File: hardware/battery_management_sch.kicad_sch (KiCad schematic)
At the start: 79 parts, among them IC1 BQ7791501PWR, IC2 BQ24618RGER, Q100 DMP3036SSD, Q2 PMOS, U1 RQ3E100BN, U2 RQ3E100BN, U3 RQ3E100BN, U4 RQ3E100BN

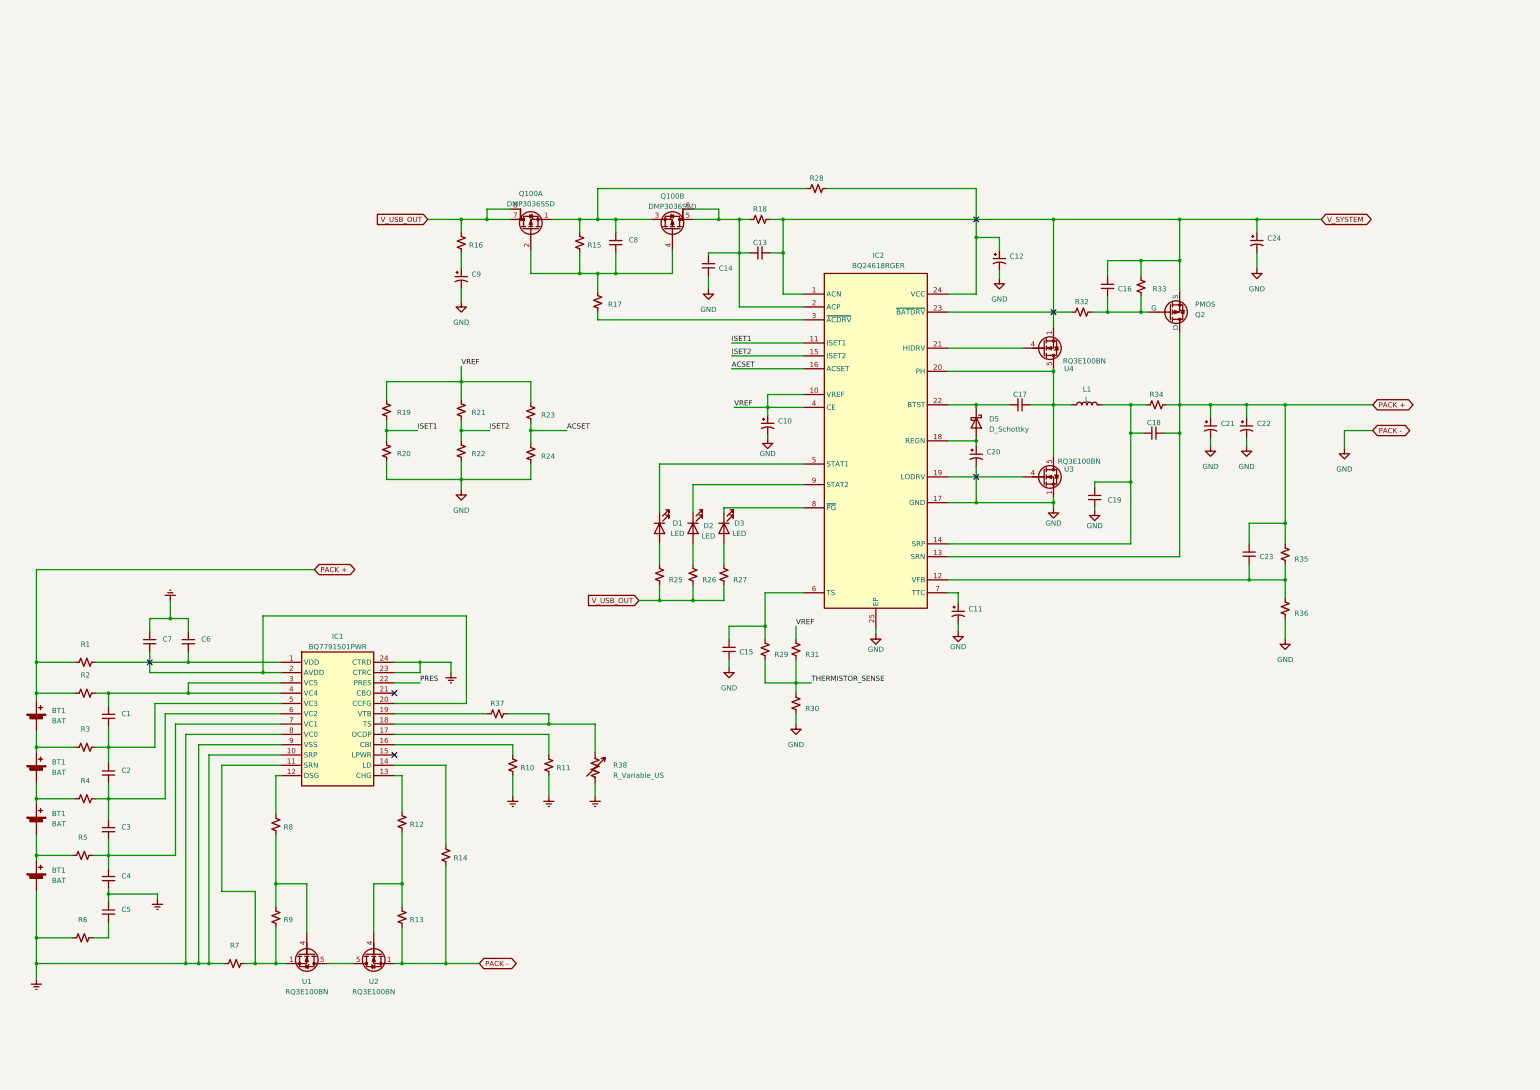
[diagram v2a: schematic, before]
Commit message: Component values chosen for bat. charge, bat. protect, USB input
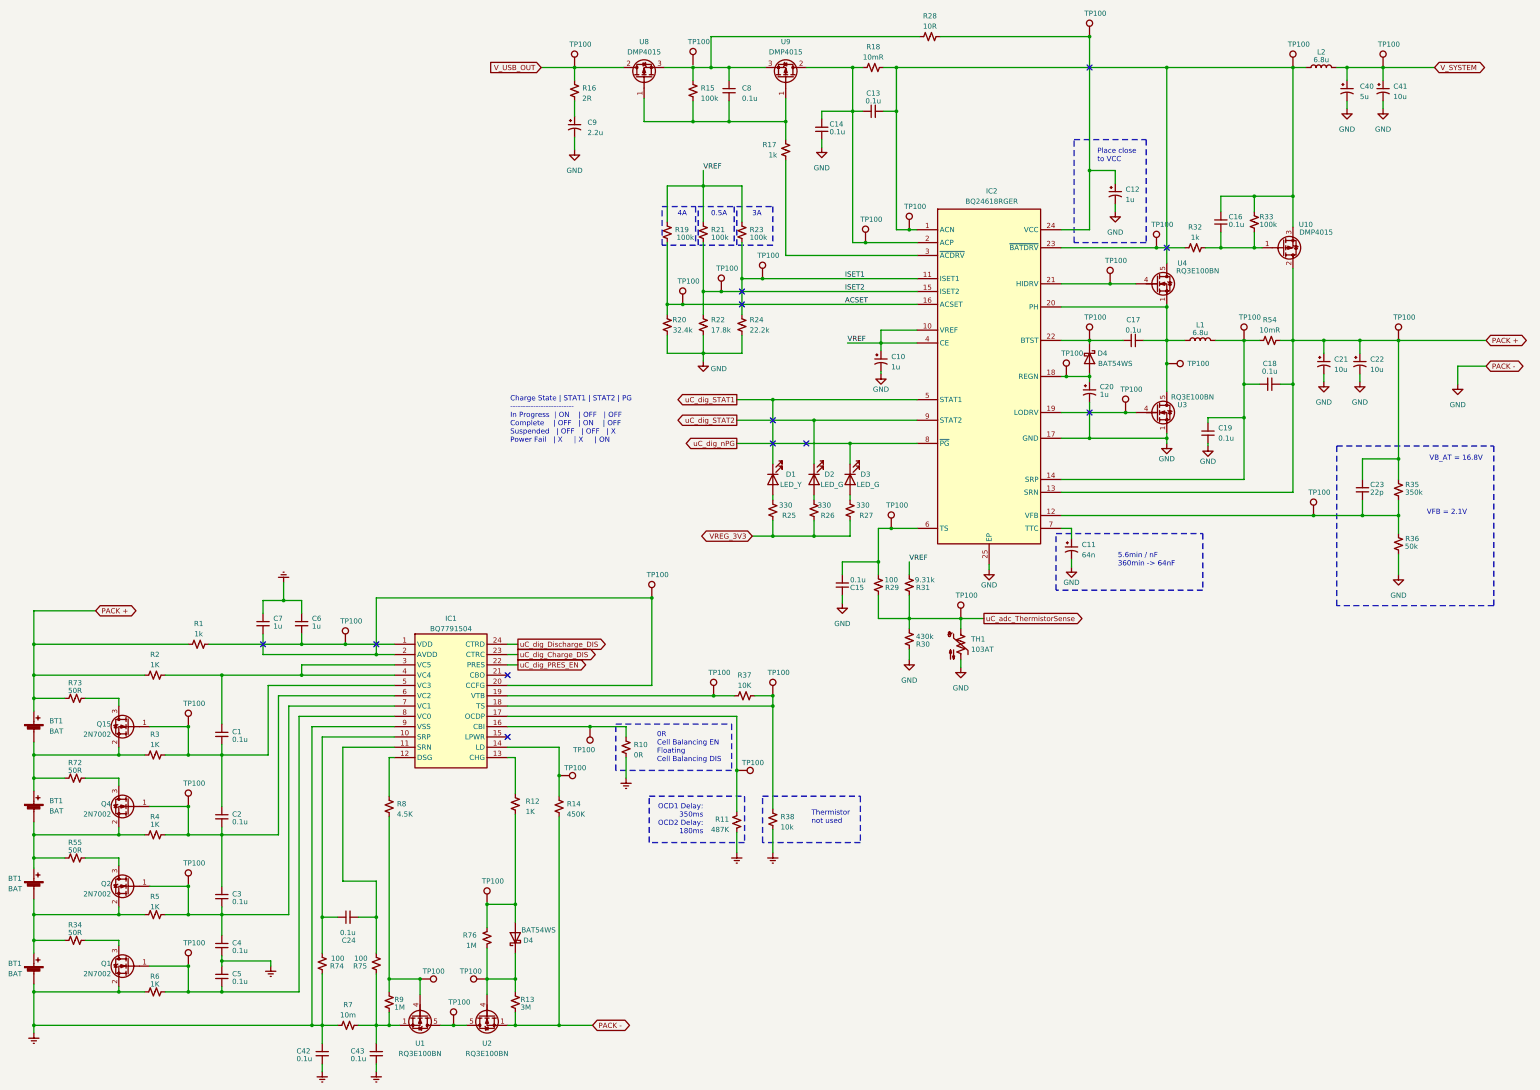
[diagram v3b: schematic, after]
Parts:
- removed C24: ~, symbol Device:C_Polarized_Small_US
- removed D5: D_Schottky, symbol Device:D_Schottky
- removed Q100: DMP3036SSD, Package_SO:SO-8_3.9x4.9mm_P1.27mm, symbol Device:Q_Dual_PMOS_S1G1S2G2D2D2D1D1
- removed Q2: PMOS, symbol Simulation_SPICE:PMOS
- removed R38: R_Variable_US, symbol Device:R_Variable_US
- added C24, C42, C43: 0.1u, Capacitor_SMD:C_0805_2012Metric, symbol Device:C_Small
- added C40: 5u, symbol Device:C_Polarized_Small_US
- added C41: 10u, symbol Device:C_Polarized_Small_US
- added D4 (x2): BAT54WS, Diode_SMD:D_SOD-323_HandSoldering, symbol Device:D_Schottky
- added L2: 6.8u, Inductor_SMD:L_Bourns_SRR1260, symbol Device:L
- added Q1, Q15, Q2, Q4: 2N7002, Package_TO_SOT_SMD:SOT-23, symbol Transistor_FET:2N7002
- added R38: 10k, symbol Device:R_Small_US
- added R54: 10mR, Resistor_SMD:R_1206_3216Metric, symbol Device:R_Small_US
- added R55, R72, R73: 50R, symbol Device:R_Small_US
- added R74, R75: 100, symbol Device:R_Small_US
- added R76: 1M, symbol Device:R_Small_US
- added TH1: 103AT, User_Thermistor:Thermistor_AWG30, symbol Device:Thermistor_NTC_US
- added TP100 (x36): ~, TestPoint:TestPoint_Pad_D1.5mm, symbol Connector:TestPoint
- added U10, U8, U9: DMP4015, Package_TO_SOT_SMD:TO-252-2, symbol User_MOSFET:DMP4015
- C1, C2, C3, C4, C5: value ~ -> 0.1u; footprint (none) -> Capacitor_SMD:C_0805_2012Metric
- C10, C12, C20, C6, C7: value ~ -> 1u
- C11: value ~ -> 64n
- C13, C14, C15, C16, C17, C18, C19, C8: value ~ -> 0.1u
- C21, C22: value ~ -> 10u
- C23: value ~ -> 22p
- C9: value ~ -> 2.2u
- D1: value LED -> LED_Y; footprint (none) -> LED_SMD:LED_0805_2012Metric_Pad1.15x1.40mm_HandSolder
- D2: value LED -> LED_G
- D3: value LED -> LED_G; footprint (none) -> LED_SMD:LED_0805_2012Metric_Pad1.15x1.40mm_HandSolder
- IC1: value BQ7791501PWR -> BQ7791504; Height 1.2 -> (none); Manufacturer_Name Texas Instruments -> (none); Manufacturer_Part_Number BQ7791501PWR -> (none); Mouser Part Number 595-BQ7791501PWR -> 595-BQ7791504PW; Mouser Price/Stock https://www.mouser.co.uk/ProductDetail/Texas-Instruments/BQ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 -> https://www.mouser.com/ProductDetail/Texas-Instruments/BQ77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; Price (none) -> 2.11
- L1: value L -> 6.8u; footprint (none) -> Inductor_SMD:L_Bourns_SRR1260; Price (none) -> 0.58; Vendor (none) -> https://www.mouser.com/ProductDetail/Bourns/SRR1260A-6R8Y?q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
- R1, R17, R32: value ~ -> 1k
- R10: value ~ -> 0R
- R11: value ~ -> 487K
- R12, R2, R3, R4, R5, R6: value ~ -> 1K
- R13: value ~ -> 3M
- R14: value ~ -> 450K
- R15, R19, R21, R23, R33: value ~ -> 100k
- R16: value ~ -> 2R; footprint (none) -> Resistor_SMD:R_2010_5025Metric
- R18: value ~ -> 10mR; footprint (none) -> Resistor_SMD:R_1206_3216Metric
- R20: value ~ -> 32.4k
- R22: value ~ -> 17.8k
- R24: value ~ -> 22.2k
- R25, R26, R27: value ~ -> 330
- R28: value ~ -> 10R
- R29: value ~ -> 100
- R30: value ~ -> 430k
- R31: value ~ -> 9.31k
- R34: value ~ -> 50R
- R35: value ~ -> 350k
- R36: value ~ -> 50k
- R37: value ~ -> 10K
- R7: value ~ -> 10m
- R8: value ~ -> 4.5K
- R9: value ~ -> 1M
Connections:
- net ACSET: now also R19.2, R20.1, TP100.1; no longer R23.2, R24.1
- net Earth: now also C42.1, C42.2, C43.2, Q1.2 (S), R38.2, R74.1; no longer IC1.10 (SRP), IC1.23 (CTRC), IC1.24 (CTRD), IC1.8 (VC0)
- net GND: now also C40.2, C41.2, TH1.2
- net ISET1: now also R23.2, R24.1, TP100.1; no longer R19.2, R20.1
- net ISET2: now also TP100.1
- net PACK +: now also R54.2, R73.1, TP100.1, U10.2; no longer R34.2
- net V_SYSTEM: now also C40.1, C41.1, L2.2, TP100.1; no longer C13.2, C16.2, IC2.1 (ACN), R18.2, R33.2, U4.1, U4.2, U4.3
- net V_USB_OUT: now also TP100.1, U8.2; no longer R25.1, R26.1, R27.1
- net at C17.2, IC2.22 (BTST): now also D4.1 (K), TP100.1
- net at C20.1, IC2.18 (REGN): now also D4.2 (A), TP100.1
- net at C16.1, R32.2, R33.1: now also U10.1
- net at C8.1, R15.2, R28.1: now also U8.3, U9.3
- net at C8.2, R15.1, R17.1: now also U8.1, U9.1
- net at C13.1, C14.2, IC2.2 (ACP)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: now also TP100.1, U9.2
- net at IC2.19 (LODRV), U3.4: now also TP100.1
- net at C17.1, IC2.20 (PH), L1.1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: now also U4.1, U4.2, U4.3, TP100.1; no longer U4.5
- net at BT1.1 (+), BT1.2 (-), R3.1: now also Q15.2 (S), R72.1
- net at C1.2, C2.1, IC1.5 (VC3)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: now also Q15.1 (G), TP100.1
- net at C23.2, IC2.12 (VFB), R35.1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: now also TP100.1
- net at C15.2, IC2.6 (TS), R29.2: now also TP100.1
- net at R13.2, U2.4: now also D4.1 (K), R76.1, TP100.1; no longer R12.1
- net at U1.5, U2.5: now also TP100.1
- net at BT1.1 (+), BT1.2 (-), R4.1: now also Q4.2 (S), R55.1
- net at BT1.1 (+), BT1.2 (-), R5.1: now also R34.1, Q2.2 (S)
- net at C5.2, R6.2: now also IC1.8 (VC0), Q1.1 (G), TP100.1
- net at R7.2, R9.1, U1.1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: now also C43.1, R75.2; no longer IC1.11 (SRN)
- net at R8.1, R9.2, U1.4: now also TP100.1
- net uC_dig_nPG: now reaches D3.1 (K), IC2.8 (~{PG})
- net uC_dig_STAT2: now reaches D2.1 (K), IC2.9 (STAT2)
- net at IC1.14 (LD), R14.2: now also TP100.1
- net at IC2.23 (~{BATDRV}), R32.1: now also TP100.1
- net at C6.2, IC1.1 (VDD), R1.2: now also TP100.1
- net at C2.2, C3.1, IC1.6 (VC2)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: now also Q4.1 (G), TP100.1
- net at C3.2, C4.1, IC1.7 (VC1)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: now also Q2.1 (G), TP100.1
- net at IC1.17 (OCDP), R11.1: now also TP100.1
- net at C7.2, IC1.2 (AVDD), IC1.20 (CCFG): now also TP100.1
- net at C12.1, IC2.24 (VCC), R28.2: now also TP100.1
- net uC_dig_STAT1: now reaches D1.1 (K), IC2.5 (STAT1)
- net at IC1.19 (VTB), R37.1: now also TP100.1
- net at IC1.18 (TS), R37.2: now also R38.1, TP100.1
- net at C18.2, C19.1, IC2.14 (SRP)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: now also R54.1, TP100.1; no longer R34.1
- net at IC1.16 (CBI), R10.1: now also TP100.1
- net at IC2.21 (HIDRV), U4.4: now also TP100.1
- net PRES renamed uC_dig_PRES_EN
- net THERMISTOR_SENSE renamed uC_adc_ThermistorSense
- net uC_adc_ThermistorSense: now also TH1.1, TP100.1
- new net: Q2.3 (D), R55.2
- new net: Q1.3 (D), R34.2
- new net: C24.2, IC1.11 (SRN), R75.1
- new net: D4.2 (A), R12.1, R76.2, TP100.1
- new net: C13.2, C16.2, IC2.1 (ACN), L2.1, R18.2, R33.2, TP100.1, TP100.1, U10.3, U4.5
- new net: Q4.3 (D), R72.2
- new net: C24.1, IC1.10 (SRP), R74.2
- new net: Q15.3 (D), R73.2
- new net VREG_3V3: R25.1, R26.1, R27.1
- new net uC_dig_Charge_DIS: IC1.23 (CTRC)
- new net uC_dig_Discharge_DIS: IC1.24 (CTRD)
- no-connect marks 6 -> 12
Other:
- note added: "0.5A"
- note added: "0R Cell Balancing EN Floating Cell Balancing DIS"
- note added: "3A"
- note added: "4A"
- note added: "5.6min / nF 360min -> 64nF"
- note added: "Charge State | STAT1 | STAT2 | PG ------------------------- In Progress | ON | OFF | OFF Complete | OFF | ON | OFF Suspended | OFF | OFF | X Power Fail | X | X | ON"
- note added: "OCD1 Delay: 350ms OCD2 Delay: 180ms"
- note added: "Place close to VCC"
- note added: "Thermistor not used"
- note added: "VB_AT = 16.8V"
- note added: "VFB = 2.1V"
- moved on the sheet: BT1, C1, C10, C11, C12, C13, C14, C15, C16, C17, C18, C19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

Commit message: Most work finished on stage1. Moving on to stage2.
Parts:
- removed L2: 6.8u, Inductor_SMD:L_Bourns_SRR1260, symbol Device:L
- added C44: 0.1u, symbol Device:C_Small
- added D9: D_Zener, symbol Device:D_Zener
- added R77: 50k, symbol Device:R_Small_US
- added R78: 8.8k, symbol Device:R_Small_US
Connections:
- net GND: now also C44.1, D9.2 (A), R78.1
- net V_SYSTEM: now also C13.2, C16.2, IC2.1 (ACN), R18.2, R33.2, TP100.1, TP100.1, U10.3, U4.5
- net V_USB_OUT: now also R77.2
- new net uc_an_usbVoltage: C44.2, D9.1 (K), R77.1, R78.2
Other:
- title: (none) -> Battery Management Stage

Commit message: More simulation and work done on SEPIC stage. MOSFET changes to USB stage and charging stage.
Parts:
- removed U10, U8, U9: DMP4015, Package_TO_SOT_SMD:TO-252-2, symbol User_MOSFET:DMP4015
- added Q10: SQJ951EP, Daniel_xMOS:PowerPAK® SO-8L Dual, symbol Daniel_PMOS:Q_Dual_PMOS_S1G1S2G2D2D1
- added Q13: STL45P3LLH6, Daniel_xMOS:PowerFLAT 5x6, symbol Daniel_PMOS:Q_PMOS_DGS
- added Q6: MUN5334DW1, Package_TO_SOT_SMD:SOT-363_SC-70-6, symbol Transistor_BJT:MUN5334DW1
- added R42, R52: R_Small_US, symbol Device:R_Small_US
- D3: value LED_G -> LED_R
- renumbered BT1 to BT2, BT1 to BT3, BT1 to BT4, D4 to D5, D4 to D8, TP100 to TP1, TP100 to TP10, TP100 to TP11, TP100 to TP12, TP100 to TP13, TP100 to TP14, TP100 to TP15, TP100 to TP16, TP100 to TP17, TP100 to TP18, TP100 to TP19, TP100 to TP2, TP100 to TP20, TP100 to TP21, TP100 to TP22, TP100 to TP23, TP100 to TP24, TP100 to TP25, TP100 to TP26, TP100 to TP27, TP100 to TP28, TP100 to TP29, TP100 to TP3, TP100 to TP30, TP100 to TP31, TP100 to TP32, TP100 to TP33, TP100 to TP34, TP100 to TP35, TP100 to TP36, TP100 to TP4, TP100 to TP5, TP100 to TP6, TP100 to TP7, TP100 to TP8, TP100 to TP9
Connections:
- net GND: now also Q6.1 (E2), R52.1
- net PACK +: now also Q13.5 (D), Q13.6 (D), Q13.7 (G), Q13.8 (D), Q6.4 (E1)
- net V_SYSTEM: now also Q13.1 (S), Q13.2 (D), Q13.3 (D)
- net V_USB_OUT: now also Q10.6
- net at C13.1, C14.2, IC2.2 (ACP)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: now also Q10.5
- net at C8.2, R15.1, R17.1: now also Q10.2, Q10.4
- net at C8.1, R15.2, R28.1: now also TP1.1, Q10.1, Q10.3
- net at C16.1, R32.2, R33.1: now also Q13.7 (G)
- new net: Q6.3 (C1), R42.2
- new net: Q6.5 (B1), Q6.6 (C2)
- new net gAnBatteryMeas: R42.1, R52.2
- new net gDigBarreryMeas_En: Q6.2 (B2)
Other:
- moved on the sheet: R17, R28, TP1, TP4

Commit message: Saving prior to changing project structure
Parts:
- removed Q1, Q15, Q2, Q4: 2N7002, Package_TO_SOT_SMD:SOT-23, symbol Transistor_FET:2N7002
- added U10, U12, U8, U9: T2N7002AK, Package_TO_SOT_SMD:SOT-23, symbol User_MOSFET:T2N7002AK,LM
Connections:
- net Earth: now also U12.2
- net at BT1.2 (-), BT2.1 (+), R3.1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: now also U8.2
- net at C1.2, C2.1, IC1.5 (VC3)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: now also U8.1
- net at BT2.2 (-), BT3.1 (+), R4.1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: now also U9.2
- net at R55.2: now also U10.3
- net at BT3.2 (-), BT4.1 (+), R34.1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: now also U10.2
- net at R34.2: now also U12.3
- net at C3.2, C4.1, IC1.7 (VC1)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: now also U10.1
- net at C5.2, IC1.8 (VC0), R6.2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: now also U12.1
- net at C2.2, C3.1, IC1.6 (VC2)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: now also U9.1
- net at R72.2: now also U9.3
- net at R73.2: now also U8.3
